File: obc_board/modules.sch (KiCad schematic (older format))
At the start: 25 parts

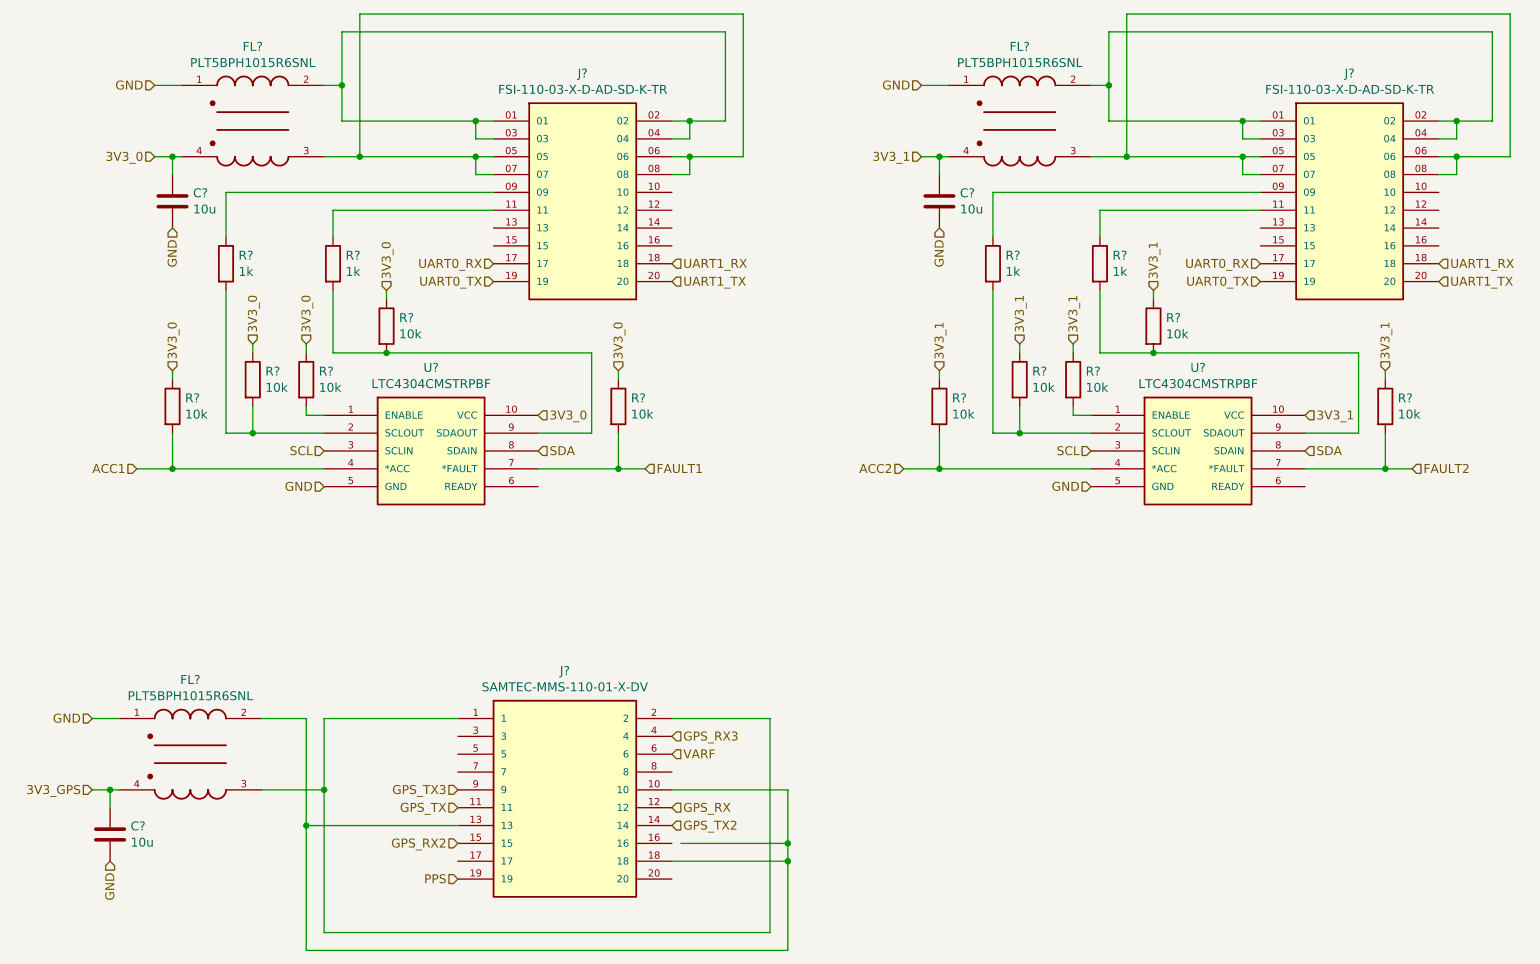
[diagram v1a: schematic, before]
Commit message: updated footprints
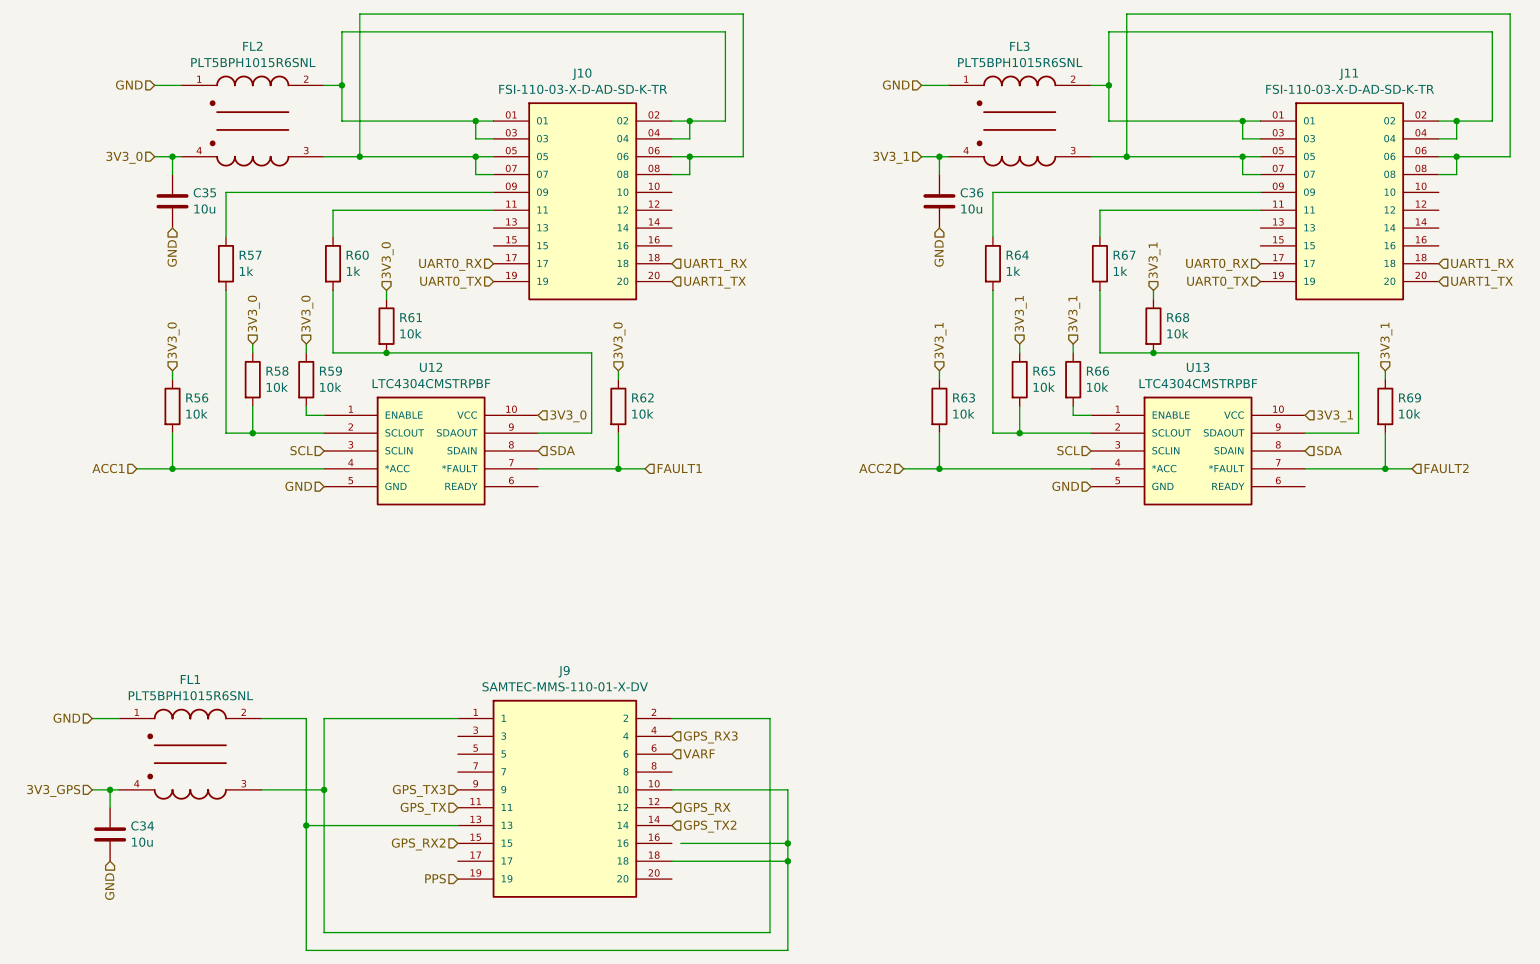
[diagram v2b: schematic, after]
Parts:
- J10, J11: renamed from J?; footprint SAMTEC_FSI-110-03-X-D-AD-SD-K-TR -> cubesat_obc:SAMTEC_FSI-110-10-X-D-AD-TR; Digikey Part Number (none) -> SAM9412-ND
- J9: renamed from J?; footprint SAMTEC-MMS-110-01-X-DV -> cubesat_obc:SAMTEC-MMS-110-01-X-DV; Digikey Part Number (none) -> MMS-110-01-F-DV-ND
- U12, U13: renamed from U?; footprint MSOP-10_MS -> Package_SO:MSOP-10_3x3mm_P0.5mm; Digikey Part Number (none) -> LTC4304CMS#PBF-ND
- gave numbers to parts that had none: 20
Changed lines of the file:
@@
 $EndDescr
 $Comp
-L cubesat_obc_lib:FSI-110-03-X-D-AD-SD-K-TR J?
+L cubesat_obc_lib:FSI-110-03-X-D-AD-SD-K-TR J10
 U 1 1 5FA42BE1
 P 4550 3000
-F 0 "J?" H 4550 3767 50  0000 C CNN
+F 0 "J10" H 4550 3767 50  0000 C CNN
 F 1 "FSI-110-03-X-D-AD-SD-K-TR" H 4550 3676 50  0000 C CNN
-F 2 "SAMTEC_FSI-110-03-X-D-AD-SD-K-TR" H 4550 3000 50  0001 L BNN
-F 3 "4.4mm" H 4550 3000 50  0001 L BNN
+F 2 "cubesat_obc:SAMTEC_FSI-110-10-X-D-AD-TR" H 4550 3000 50  0001 L BNN
+F 3 "http://suddendocs.samtec.com/prints/fsi-1xx-03-x-d-x-xx-xx-footprint.pdf" H 4550 3000 50  0001 L BNN
 F 4 "Manufacturer Recommendations" H 4550 3000 50  0001 L BNN "Field4"
 F 5 "Samtec" H 4550 3000 50  0001 L BNN "Field5"
 F 6 "P" H 4550 3000 50  0001 L BNN "Field6"
+F 7 "SAM9412-ND" H 4550 3000 50  0001 C CNN "Digikey Part Number"
 	1    4550 3000
 	1    0    0    -1
@@
 	2150 2700 2250 2700
 $Comp
-L Device:C C?
+L Device:C C35
 U 1 1 5FA44CB1
 P 2250 2950
-F 0 "C?" H 2365 2996 50  0000 L CNN
+F 0 "C35" H 2365 2996 50  0000 L CNN
 F 1 "10u" H 2365 2905 50  0000 L CNN
 F 2 "" H 2288 2800 50  0001 C CNN
@@
 	2250 2700 2250 2800
 $Comp
-L cubesat_obc_lib:PLT5BPH1015R6SNL FL?
+L cubesat_obc_lib:PLT5BPH1015R6SNL FL2
 U 1 1 5FA4787C
 P 2700 2500
-F 0 "FL?" H 2700 2917 50  0000 C CNN
+F 0 "FL2" H 2700 2917 50  0000 C CNN
 F 1 "PLT5BPH1015R6SNL" H 2700 2826 50  0000 C CNN
 F 2 "FIL_PLT5BPH1015R6SNL" H 2700 2500 50  0001 L BNN
@@
 P 2150 4200
 AR Path="/5F315FB6/5FA51727" Ref="U?"  Part="1"
-AR Path="/5FA4220C/5FA51727" Ref="U?"  Part="1"
-F 0 "U?" H 3700 4517 50  0000 C CNN
+AR Path="/5FA4220C/5FA51727" Ref="U12"  Part="1"
+F 0 "U12" H 3700 4517 50  0000 C CNN
 F 1 "LTC4304CMSTRPBF" H 3700 4426 50  0000 C CNN
-F 2 "MSOP-10_MS" H 3100 4250 50  0001 L BNN
-F 3 "ltc4304cms#trpbf" H 3100 4250 50  0001 L BNN
+F 2 "Package_SO:MSOP-10_3x3mm_P0.5mm" H 3100 4250 50  0001 L BNN
+F 3 "http://www.linear.com/docs/16798" H 3100 4250 50  0001 L BNN
 F 4 "Linear Technology" H 3100 4250 50  0001 L BNN "Field4"
+F 5 "LTC4304CMS#PBF-ND" H 2150 4200 50  0001 C CNN "Digikey Part Number"
 	1    2150 4200
 	1    0    0    -1
@@
 P 3000 3950
 AR Path="/5F315FB6/5FA51731" Ref="R?"  Part="1"
-AR Path="/5FA4220C/5FA51731" Ref="R?"  Part="1"
-F 0 "R?" H 3070 3996 50  0000 L CNN
+AR Path="/5FA4220C/5FA51731" Ref="R59"  Part="1"
+F 0 "R59" H 3070 3996 50  0000 L CNN
 F 1 "10k" H 3070 3905 50  0000 L CNN
 F 2 "" V 2930 3950 50  0001 C CNN
@@
 P 2250 4100
 AR Path="/5F315FB6/5FA5173F" Ref="R?"  Part="1"
-AR Path="/5FA4220C/5FA5173F" Ref="R?"  Part="1"
-F 0 "R?" H 2320 4146 50  0000 L CNN
+AR Path="/5FA4220C/5FA5173F" Ref="R56"  Part="1"
+F 0 "R56" H 2320 4146 50  0000 L CNN
 F 1 "10k" H 2320 4055 50  0000 L CNN
 F 2 "" V 2180 4100 50  0001 C CNN
@@
 P 4750 4100
 AR Path="/5F315FB6/5FA5174A" Ref="R?"  Part="1"
-AR Path="/5FA4220C/5FA5174A" Ref="R?"  Part="1"
-F 0 "R?" H 4820 4146 50  0000 L CNN
+AR Path="/5FA4220C/5FA5174A" Ref="R62"  Part="1"
+F 0 "R62" H 4820 4146 50  0000 L CNN
 F 1 "10k" H 4820 4055 50  0000 L CNN
 F 2 "" V 4680 4100 50  0001 C CNN
@@
 P 3450 3650
 AR Path="/5F315FB6/5FA5ADB3" Ref="R?"  Part="1"
-AR Path="/5FA4220C/5FA5ADB3" Ref="R?"  Part="1"
-F 0 "R?" H 3520 3696 50  0000 L CNN
+AR Path="/5FA4220C/5FA5ADB3" Ref="R61"  Part="1"
+F 0 "R61" H 3520 3696 50  0000 L CNN
 F 1 "10k" H 3520 3605 50  0000 L CNN
 F 2 "" V 3380 3650 50  0001 C CNN
@@
 P 2700 3950
 AR Path="/5F315FB6/5FA5BDA5" Ref="R?"  Part="1"
-AR Path="/5FA4220C/5FA5BDA5" Ref="R?"  Part="1"
-F 0 "R?" H 2770 3996 50  0000 L CNN
+AR Path="/5FA4220C/5FA5BDA5" Ref="R58"  Part="1"
+F 0 "R58" H 2770 3996 50  0000 L CNN
 F 1 "10k" H 2770 3905 50  0000 L CNN
 F 2 "" V 2630 3950 50  0001 C CNN
@@
 P 2550 3300
 AR Path="/5F315FB6/5FA7F305" Ref="R?"  Part="1"
-AR Path="/5FA4220C/5FA7F305" Ref="R?"  Part="1"
-F 0 "R?" H 2620 3346 50  0000 L CNN
+AR Path="/5FA4220C/5FA7F305" Ref="R57"  Part="1"
+F 0 "R57" H 2620 3346 50  0000 L CNN
 F 1 "1k" H 2620 3255 50  0000 L CNN
 F 2 "" V 2480 3300 50  0001 C CNN
@@
 P 3150 3300
 AR Path="/5F315FB6/5FA89462" Ref="R?"  Part="1"
-AR Path="/5FA4220C/5FA89462" Ref="R?"  Part="1"
-F 0 "R?" H 3220 3346 50  0000 L CNN
+AR Path="/5FA4220C/5FA89462" Ref="R60"  Part="1"
+F 0 "R60" H 3220 3346 50  0000 L CNN
 F 1 "1k" H 3220 3255 50  0000 L CNN
 F 2 "" V 3080 3300 50  0001 C CNN
@@
 UART1_TX
 $Comp
-L cubesat_obc_lib:FSI-110-03-X-D-AD-SD-K-TR J?
+L cubesat_obc_lib:FSI-110-03-X-D-AD-SD-K-TR J11
 U 1 1 5FAAED71
 P 8850 3000
-F 0 "J?" H 8850 3767 50  0000 C CNN
+F 0 "J11" H 8850 3767 50  0000 C CNN
 F 1 "FSI-110-03-X-D-AD-SD-K-TR" H 8850 3676 50  0000 C CNN
-F 2 "SAMTEC_FSI-110-03-X-D-AD-SD-K-TR" H 8850 3000 50  0001 L BNN
-F 3 "4.4mm" H 8850 3000 50  0001 L BNN
+F 2 "cubesat_obc:SAMTEC_FSI-110-10-X-D-AD-TR" H 8850 3000 50  0001 L BNN
+F 3 "http://suddendocs.samtec.com/prints/fsi-1xx-03-x-d-x-xx-xx-footprint.pdf" H 8850 3000 50  0001 L BNN
 F 4 "Manufacturer Recommendations" H 8850 3000 50  0001 L BNN "Field4"
 F 5 "Samtec" H 8850 3000 50  0001 L BNN "Field5"
 F 6 "P" H 8850 3000 50  0001 L BNN "Field6"
+F 7 "SAM9412-ND" H 8850 3000 50  0001 C CNN "Digikey Part Number"
 	1    8850 3000
 	1    0    0    -1
@@
 	6450 2700 6550 2700
 $Comp
-L Device:C C?
+L Device:C C36
 U 1 1 5FAAED7A
 P 6550 2950
-F 0 "C?" H 6665 2996 50  0000 L CNN
+F 0 "C36" H 6665 2996 50  0000 L CNN
 F 1 "10u" H 6665 2905 50  0000 L CNN
 F 2 "" H 6588 2800 50  0001 C CNN
@@
 	6550 2700 6550 2800
 $Comp
-L cubesat_obc_lib:PLT5BPH1015R6SNL FL?
+L cubesat_obc_lib:PLT5BPH1015R6SNL FL3
 U 1 1 5FAAED86
 P 7000 2500
-F 0 "FL?" H 7000 2917 50  0000 C CNN
+F 0 "FL3" H 7000 2917 50  0000 C CNN
 F 1 "PLT5BPH1015R6SNL" H 7000 2826 50  0000 C CNN
 F 2 "FIL_PLT5BPH1015R6SNL" H 7000 2500 50  0001 L BNN
@@
 P 6450 4200
 AR Path="/5F315FB6/5FAAED92" Ref="U?"  Part="1"
-AR Path="/5FA4220C/5FAAED92" Ref="U?"  Part="1"
-F 0 "U?" H 8000 4517 50  0000 C CNN
+AR Path="/5FA4220C/5FAAED92" Ref="U13"  Part="1"
+F 0 "U13" H 8000 4517 50  0000 C CNN
 F 1 "LTC4304CMSTRPBF" H 8000 4426 50  0000 C CNN
-F 2 "MSOP-10_MS" H 7400 4250 50  0001 L BNN
-F 3 "ltc4304cms#trpbf" H 7400 4250 50  0001 L BNN
+F 2 "Package_SO:MSOP-10_3x3mm_P0.5mm" H 7400 4250 50  0001 L BNN
+F 3 "http://www.linear.com/docs/16798" H 7400 4250 50  0001 L BNN
 F 4 "Linear Technology" H 7400 4250 50  0001 L BNN "Field4"
+F 5 "LTC4304CMS#PBF-ND" H 6450 4200 50  0001 C CNN "Digikey Part Number"
 	1    6450 4200
 	1    0    0    -1
@@
 P 7300 3950
 AR Path="/5F315FB6/5FAAED9A" Ref="R?"  Part="1"
-AR Path="/5FA4220C/5FAAED9A" Ref="R?"  Part="1"
-F 0 "R?" H 7370 3996 50  0000 L CNN
+AR Path="/5FA4220C/5FAAED9A" Ref="R66"  Part="1"
+F 0 "R66" H 7370 3996 50  0000 L CNN
 F 1 "10k" H 7370 3905 50  0000 L CNN
 F 2 "" V 7230 3950 50  0001 C CNN
@@
 P 6550 4100
 AR Path="/5F315FB6/5FAAEDA8" Ref="R?"  Part="1"
-AR Path="/5FA4220C/5FAAEDA8" Ref="R?"  Part="1"
-F 0 "R?" H 6620 4146 50  0000 L CNN
+AR Path="/5FA4220C/5FAAEDA8" Ref="R63"  Part="1"
+F 0 "R63" H 6620 4146 50  0000 L CNN
 F 1 "10k" H 6620 4055 50  0000 L CNN
 F 2 "" V 6480 4100 50  0001 C CNN
@@
 P 9050 4100
 AR Path="/5F315FB6/5FAAEDB2" Ref="R?"  Part="1"
-AR Path="/5FA4220C/5FAAEDB2" Ref="R?"  Part="1"
-F 0 "R?" H 9120 4146 50  0000 L CNN
+AR Path="/5FA4220C/5FAAEDB2" Ref="R69"  Part="1"
+F 0 "R69" H 9120 4146 50  0000 L CNN
 F 1 "10k" H 9120 4055 50  0000 L CNN
 F 2 "" V 8980 4100 50  0001 C CNN
@@
 P 7750 3650
 AR Path="/5F315FB6/5FAAEDC2" Ref="R?"  Part="1"
-AR Path="/5FA4220C/5FAAEDC2" Ref="R?"  Part="1"
-F 0 "R?" H 7820 3696 50  0000 L CNN
+AR Path="/5FA4220C/5FAAEDC2" Ref="R68"  Part="1"
+F 0 "R68" H 7820 3696 50  0000 L CNN
 F 1 "10k" H 7820 3605 50  0000 L CNN
 F 2 "" V 7680 3650 50  0001 C CNN
@@
 P 7000 3950
 AR Path="/5F315FB6/5FAAEDCA" Ref="R?"  Part="1"
-AR Path="/5FA4220C/5FAAEDCA" Ref="R?"  Part="1"
-F 0 "R?" H 7070 3996 50  0000 L CNN
+AR Path="/5FA4220C/5FAAEDCA" Ref="R65"  Part="1"
+F 0 "R65" H 7070 3996 50  0000 L CNN
 F 1 "10k" H 7070 3905 50  0000 L CNN
 F 2 "" V 6930 3950 50  0001 C CNN
@@
 P 6850 3300
 AR Path="/5F315FB6/5FAAEDD8" Ref="R?"  Part="1"
-AR Path="/5FA4220C/5FAAEDD8" Ref="R?"  Part="1"
-F 0 "R?" H 6920 3346 50  0000 L CNN
+AR Path="/5FA4220C/5FAAEDD8" Ref="R64"  Part="1"
+F 0 "R64" H 6920 3346 50  0000 L CNN
 F 1 "1k" H 6920 3255 50  0000 L CNN
 F 2 "" V 6780 3300 50  0001 C CNN
@@
 P 7450 3300
 AR Path="/5F315FB6/5FAAEDE1" Ref="R?"  Part="1"
-AR Path="/5FA4220C/5FAAEDE1" Ref="R?"  Part="1"
-F 0 "R?" H 7520 3346 50  0000 L CNN
+AR Path="/5FA4220C/5FAAEDE1" Ref="R67"  Part="1"
+F 0 "R67" H 7520 3346 50  0000 L CNN
 F 1 "1k" H 7520 3255 50  0000 L CNN
 F 2 "" V 7380 3300 50  0001 C CNN
@@
 UART1_TX
 $Comp
-L cubesat_obc_lib:SAMTEC-MMS-110-01-X-DV J?
+L cubesat_obc_lib:SAMTEC-MMS-110-01-X-DV J9
 U 1 1 5FAC7ADC
 P 4050 5850
-F 0 "J?" H 4450 6117 50  0000 C CNN
+F 0 "J9" H 4450 6117 50  0000 C CNN
 F 1 "SAMTEC-MMS-110-01-X-DV" H 4450 6026 50  0000 C CNN
-F 2 "SAMTEC-MMS-110-01-X-DV" H 4050 5850 50  0001 L BNN
-F 3 "" H 4050 5850 50  0001 C CNN
+F 2 "cubesat_obc:SAMTEC-MMS-110-01-X-DV" H 4050 5850 50  0001 L BNN
+F 3 "https://www.digikey.sg/product-detail/en/samtec-inc/MMS-110-01-F-DV/MMS-110-01-F-DV-ND/7937063" H 4050 5850 50  0001 C CNN
+F 4 "MMS-110-01-F-DV-ND" H 4050 5850 50  0001 C CNN "Digikey Part Number"
 	1    4050 5850
 	1    0    0    -1
@@
 	1800 6250 1900 6250
 $Comp
-L Device:C C?
+L Device:C C34
 U 1 1 5FACB71A
 P 1900 6500
-F 0 "C?" H 2015 6546 50  0000 L CNN
+F 0 "C34" H 2015 6546 50  0000 L CNN
 F 1 "10u" H 2015 6455 50  0000 L CNN
 F 2 "" H 1938 6350 50  0001 C CNN
@@
 	1900 6250 1900 6350
 $Comp
-L cubesat_obc_lib:PLT5BPH1015R6SNL FL?
+L cubesat_obc_lib:PLT5BPH1015R6SNL FL1
 U 1 1 5FACB726
 P 2350 6050
-F 0 "FL?" H 2350 6467 50  0000 C CNN
+F 0 "FL1" H 2350 6467 50  0000 C CNN
 F 1 "PLT5BPH1015R6SNL" H 2350 6376 50  0000 C CNN
 F 2 "FIL_PLT5BPH1015R6SNL" H 2350 6050 50  0001 L BNN

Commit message: footprints
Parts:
- C34, C35, C36: footprint (none) -> Capacitor_THT:CP_Radial_D5.0mm_P2.00mm; Digikey Part Number (none) -> 493-13398-ND
- FL1, FL2, FL3: footprint FIL_PLT5BPH1015R6SNL -> cubesat_obc:FIL_PLT5BPH1015R6SNL; Digikey Part Number (none) -> 490-10976-1-ND; Field4 PLT5BPH3013R7SNL -> (none); Field5 Unavailable -> (none); Field6 Common Mode Chokes Dual 300Ohm 10MHz 3.7A 11mOhm DCR SMD Au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 -> (none); Field7 Vertical-4 Murata -> (none); Field8 Murata -> (none)
- J10, J11: Field4 Manufacturer Recommendations -> (none); Field5 Samtec -> (none); Field6 P -> (none)
- R56, R58, R59, R61, R62, R63, R65, R66, R68, R69: footprint (none) -> Resistor_SMD:R_0402_1005Metric; Digikey Part Number (none) -> 311-10.0KLRCT-ND
- R57, R60, R64, R67: footprint (none) -> Resistor_SMD:R_0402_1005Metric; Digikey Part Number (none) -> 311-1.00KLRCT-ND
- U12, U13: Field4 Linear Technology -> (none)
